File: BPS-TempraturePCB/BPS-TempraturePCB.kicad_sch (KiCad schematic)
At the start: 39 parts, among them J1 Conn_01x24_Female, J2 TEMPSPIANALYZER, U1 MIC5317-2.5xM5, U2 LM321, U3 ADS7953SBDBT

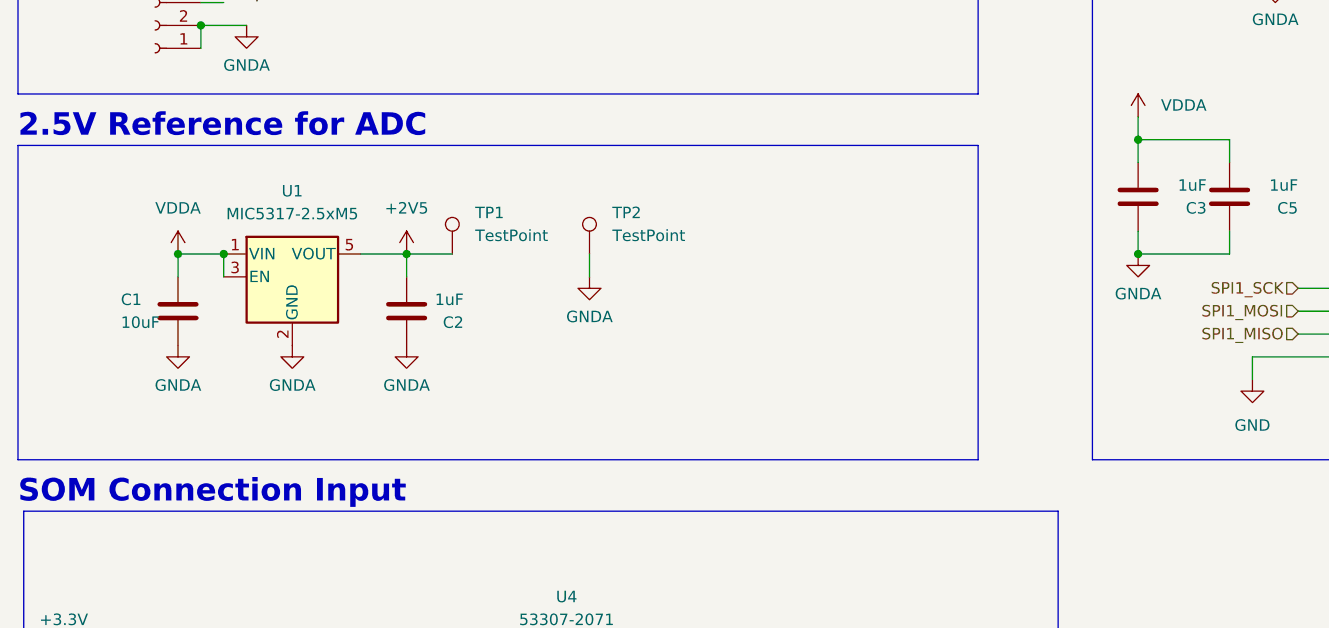
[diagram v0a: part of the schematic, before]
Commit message: All Traces connected. Need to fix silkscreen errors and add a few more test points
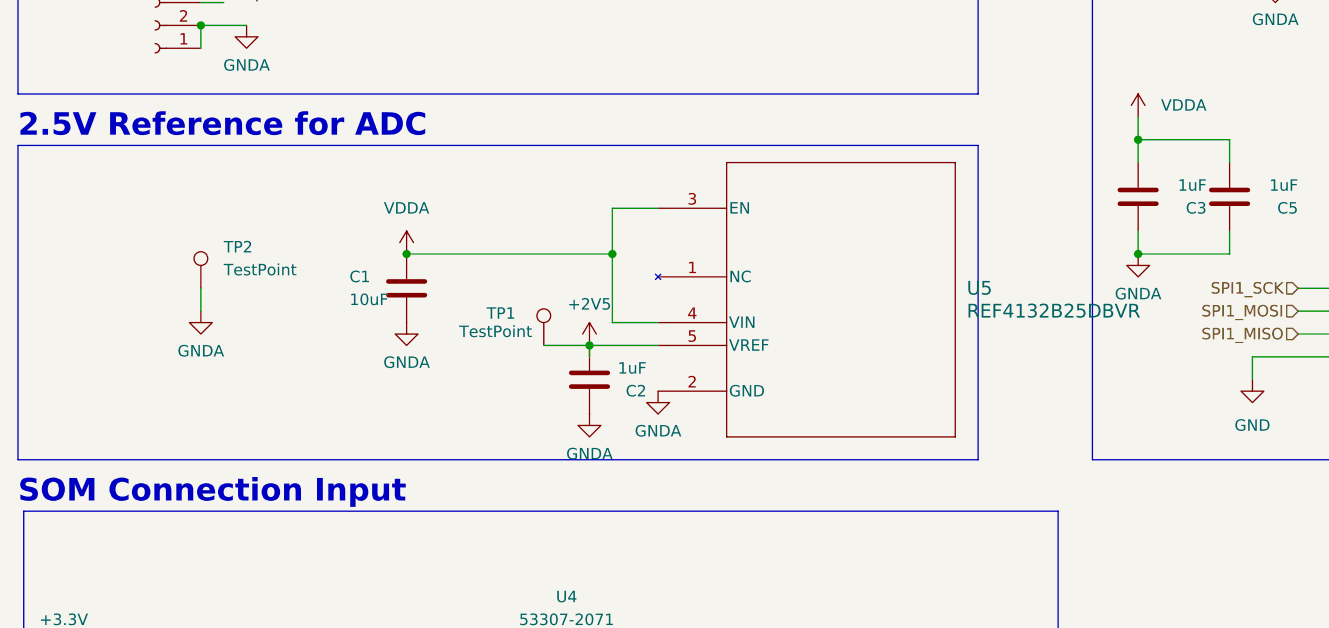
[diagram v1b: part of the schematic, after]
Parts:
- removed U1: MIC5317-2.5xM5, Package_TO_SOT_SMD:SOT-23-5, symbol Regulator_Linear:MIC5317-2.5xM5
- added U5: REF4132B25DBVR, SOT-23-5_DBV_TEX, symbol REF4132:REF4132B25DBVR
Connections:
- net +2V5: now also U5.5 (VREF)
- net GNDA: now also U5.2 (GND)
- net VDDA: now also U5.3 (EN), U5.4 (VIN)
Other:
- moved on the sheet: C1, C2, TP1, TP2

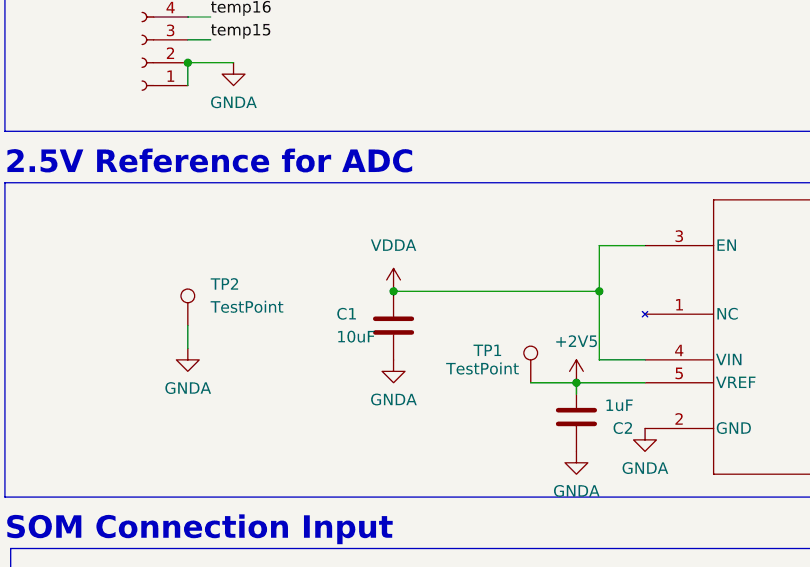
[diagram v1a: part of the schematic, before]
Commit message: added silkscreen for temprature pinheaders and testpoint for analog vdd and analog ground.
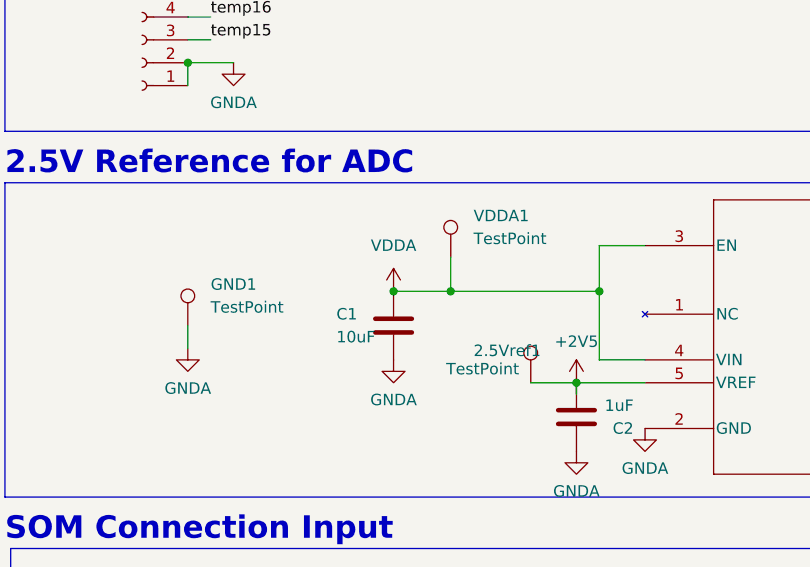
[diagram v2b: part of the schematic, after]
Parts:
- added VDDA1: TestPoint, TestPoint:TestPoint_Keystone_5005-5009_Compact, symbol Connector:TestPoint
- U5: footprint SOT-23-5_DBV_TEX -> REF4132:SOT-23-5_DBV_TEX
- renumbered TP1 to 2.5Vref1, TP2 to GND1
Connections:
- net VDDA: now also VDDA1.1
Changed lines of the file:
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@@
 	)
 	(junction
+		(at 72.39 109.22)
+		(diameter 0)
+		(color 0 0 0 0)
+	)
+	(junction
 		(at 88.9 60.96)
 		(diameter 0)
@@
 	(wire
 		(pts
+			(xy 72.39 105.41) (xy 72.39 109.22)
+		)
+		(stroke
+			(width 0)
+			(type default)
+		)
+	)
+	(wire
+		(pts
 			(xy 127 165.1) (xy 101.6 165.1)
 		)
@@
 	(wire
 		(pts
-			(xy 66.04 109.22) (xy 88.9 109.22)
+			(xy 66.04 109.22) (xy 72.39 109.22)
 		)
 		(stroke
@@
 	(wire
 		(pts
+			(xy 72.39 109.22) (xy 88.9 109.22)
+		)
+		(stroke
+			(width 0)
+			(type default)
+		)
+	)
+	(wire
+		(pts
 			(xy 167.64 48.26) (xy 165.1 48.26)
 		)
@@
 		(on_board yes)
 		(dnp no)
-		(property "Reference" "TP1"
+		(property "Reference" "2.5Vref1"
 			(at 74.93 115.824 0)
 			(effects
@@
 			(project "BPS-TempraturePCB"
 				(path "/0d13a720-80d9-4399-a39b-5c0befc79cdf"
-					(reference "TP1")
+					(reference "2.5Vref1")
 					(unit 1)
 				)
@@
 		(dnp no)
 		(fields_autoplaced yes)
-		(property "Reference" "TP2"
+		(property "Reference" "GND1"
 			(at 45.72 108.4579 0)
 			(effects
@@
 			(project "BPS-TempraturePCB"
 				(path "/0d13a720-80d9-4399-a39b-5c0befc79cdf"
-					(reference "TP2")
+					(reference "GND1")
 					(unit 1)
 				)
@@
 	)
 	(symbol
+		(lib_id "Connector:TestPoint")
+		(at 72.39 105.41 0)
+		(unit 1)
+		(exclude_from_sim no)
+		(in_bom yes)
+		(on_board yes)
+		(dnp no)
+		(fields_autoplaced yes)
+		(property "Reference" "VDDA1"
+			(at 74.93 100.8379 0)
+			(effects
+				(font
+					(size 1.27 1.27)
+				)
+				(justify left)
+			)
+		)
+		(property "Value" "TestPoint"
+			(at 74.93 103.3779 0)
+			(effects
+				(font
+					(size 1.27 1.27)
+				)
+				(justify left)
+			)
+		)
+		(property "Footprint" "TestPoint:TestPoint_Keystone_5005-5009_Compact"
+			(at 77.47 105.41 0)
+			(effects
+				(font
+					(size 1.27 1.27)
+				)
+				(hide yes)
+			)
+		)
+		(property "Datasheet" "~"
+			(at 77.47 105.41 0)
+			(effects
+				(font
+					(size 1.27 1.27)
+				)
+				(hide yes)
+			)
+		)
+		(property "Description" "test point"
+			(at 72.39 105.41 0)
+			(effects
+				(font
+					(size 1.27 1.27)
+				)
+				(hide yes)
+			)
+		)
+		(pin "1"
+		)
+		(instances
+			(project ""
+				(path "/0d13a720-80d9-4399-a39b-5c0befc79cdf"
+					(reference "VDDA1")
+					(unit 1)
+				)
+			)
+		)
+	)
+	(symbol
 		(lib_id "REF4132:REF4132B25DBVR")
 		(at 93.98 104.14 0)
@@
 			)
 		)
-		(property "Footprint" "SOT-23-5_DBV_TEX"
+		(property "Footprint" "REF4132:SOT-23-5_DBV_TEX"
 			(at 93.98 104.14 0)
 			(effects
